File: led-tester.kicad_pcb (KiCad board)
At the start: 2 copper layers, 79.7 x 19.1 mm, 19 parts, among them M1 Arduino_Mini, U1 PCF8591

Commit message: Added a current sense resistor, a decoupling cap, and rewired the PCF8591 analog inputs.
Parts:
- added C2: 100n, Capacitor_SMD:C_0805_2012Metric_Pad1.18x1.45mm_HandSolder, F.Cu at (162.1, 88.8)
- added R7: 4R7, Resistor_SMD:R_0805_2012Metric_Pad1.20x1.40mm_HandSolder, F.Cu at (162.1, 83.9)
- D4: footprint aalib:LED_D5.0mm -> Connector_PinHeader_2.54mm:PinHeader_1x02_P2.54mm_Vertical
- D5: footprint Connector_PinHeader_2.54mm:PinHeader_1x02_P2.54mm_Vertical -> aalib:LED_D5.0mm
- JP2, JP3: moved to B.Cu
- moved R1 9.90 mm to (153.6, 83.9), turned to 0 degrees
- moved R3 5.35 mm to (157.8, 83.9)
- moved D4 5.10 mm to (169.9, 90.1), turned to -90 degrees
- moved D5 5.05 mm to (169.8, 85.0), turned to 180 degrees
- moved JP2 3.70 mm to (155.4, 83.9), turned to 180 degrees
- moved JP3 3.70 mm to (152.1, 83.9)
- moved D6 2.70 mm to (162.1, 86.3)
- moved R2 1.10 mm to (162.1, 93.5)
- moved R4 1.10 mm to (162.1, 91.2)
- moved D3 0.14 mm to (168.6, 93.2)
- moved D2 0.09 mm to (168.6, 95.7)
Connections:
- C1 pad 1: /A0 -> /A2
- D1 pad 2: /VLED -> /A0
- D2 pad 2: /VLED -> /A0
- D3 pad 2: /VLED -> /A0
- D4 pad 2: /VLED -> /A0
- D5 pad 2: /VLED -> /A0
- JP1 pad 2: /VLED -> /A0
- JP2 pad 1: /A1 -> Net-(JP2-A)
- JP2 pad 2: /VLED -> /A1
- JP3 pad 2: /VLED -> /A1
- R1 pad 2: /A0 -> /A2
- R2 pad 2: /A0 -> /A2
- R3 pad 1: /A1 -> Net-(JP2-A)
- R3 pad 2: /A0 -> /A2
- U1 pad 2: /A0 -> /A1
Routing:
- net /A2: track 0.00 -> 73.6 mm
- net /VLED: track 42.0 -> 0.00 mm, vias 1 -> 0
- net /A0: track 110.7 -> 90.8 mm
- net /*D3: track 40.4 -> 24.1 mm
- net GND: track 81.9 -> 90.2 mm
- net Net-(D6-A): track 3.20 -> 8.02 mm
- net /A1: track 55.5 -> 59.9 mm, vias 1 -> 3
- net Net-(JP2-A): track 0.00 -> 2.09 mm, vias 0 -> 1
- net Net-(JP3-A): track 4.96 -> 6.85 mm, vias 0 -> 1
- net +5V: track 39.8 -> 41.4 mm
- net /A5/SCL: track 36.2 -> 36.8 mm
- net /D13/SCK: track 60.2 -> 59.7 mm
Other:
- board text added: "2-May-23"
- board text added: "mjd v1.0d"
- board text added: "nano"
- board text removed: "24-Feb-23"
- board text removed: "mjd v1.0c"

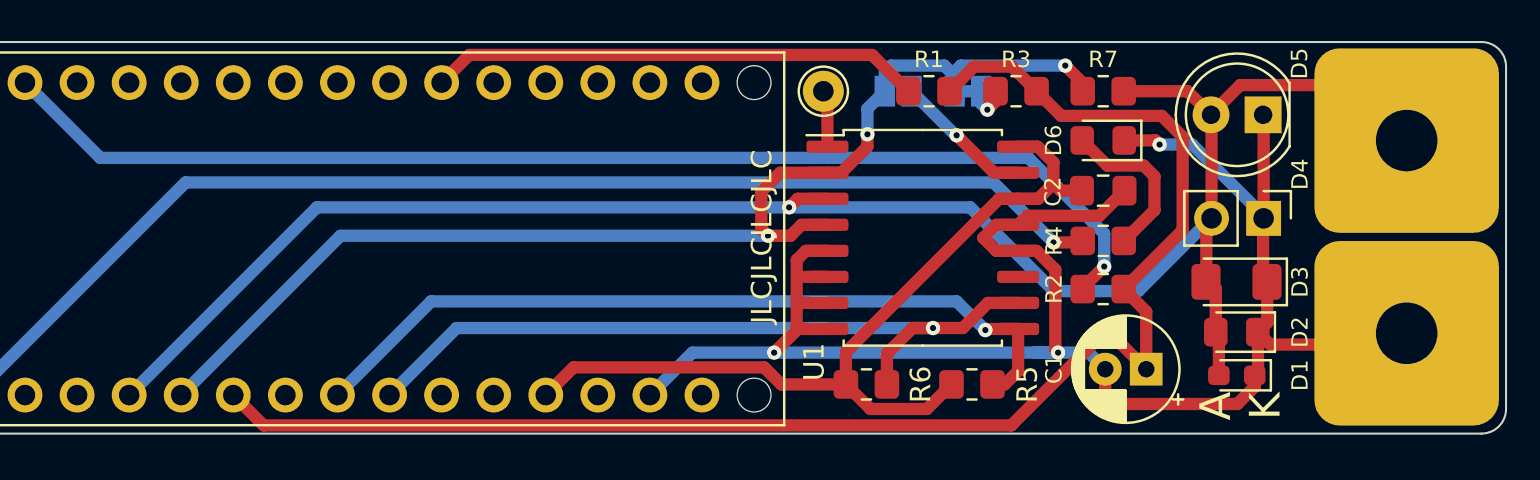
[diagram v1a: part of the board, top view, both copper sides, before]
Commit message: Added a sense resistor between the LED under test, and GND.
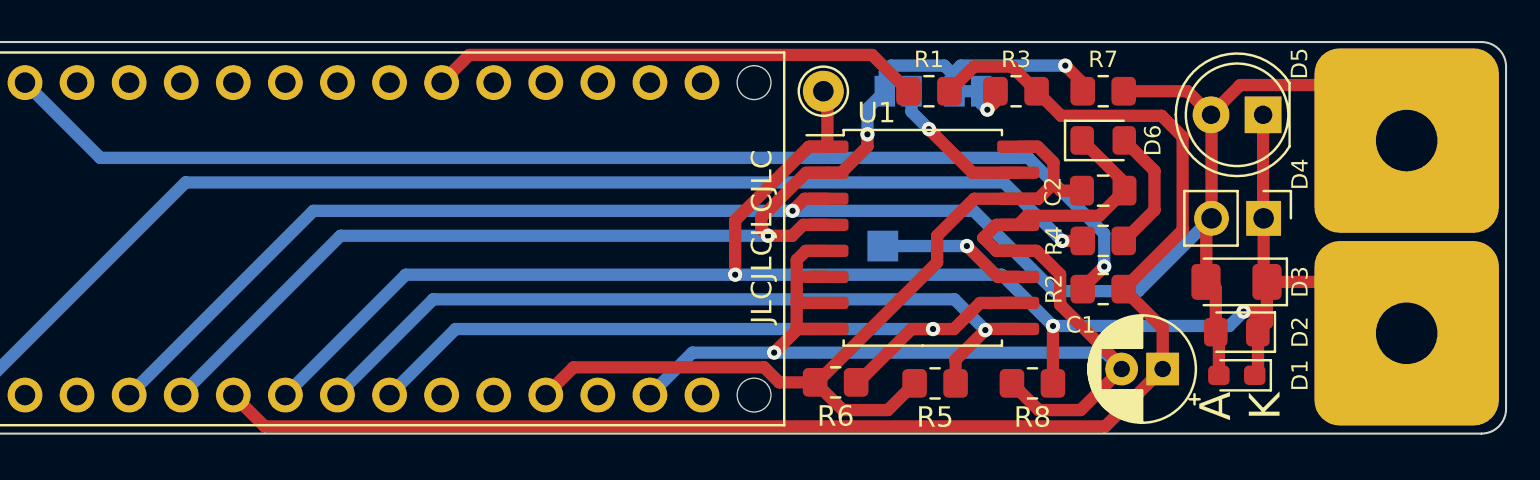
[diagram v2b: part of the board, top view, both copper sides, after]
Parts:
- added R8: 4R7, Resistor_SMD:R_0805_2012Metric_Pad1.20x1.40mm_HandSolder, F.Cu at (158.6, 98.2)
- added TP2: TestPoint, TestPoint:TestPoint_Pad_1.5x1.5mm, B.Cu at (151.3, 91.5)
- moved R5 1.80 mm to (153.8, 98.2)
- moved R6 1.50 mm to (149.0, 98.1)
- moved C1 0.80 mm to (164.9, 97.5)
- turned D6 to 0 degrees
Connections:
- D1 pad 1: GND -> /A3
- D2 pad 1: GND -> /A3
- D3 pad 1: GND -> /A3
- D4 pad 1: GND -> /A3
- D5 pad 1: GND -> /A3
- JP1 pad 1: GND -> /A3
- TP1 pad 1: Net-(U1-AIN0) -> /A3
- U1 pad 1: Net-(U1-AIN0) -> /A3
- U1 pad 11: unconnected-(U1-OSC-Pad11) -> Net-(U1-OSC)
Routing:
- net /A3: track 0.00 -> 86.8 mm, vias 0 -> 3
- net GND: track 90.2 -> 63.2 mm, vias 3 -> 1
- net Net-(U1-OSC): track 0.00 -> 7.22 mm, vias 0 -> 1
- net Net-(U1-AIN0): track 2.79 -> 0.00 mm
- net Net-(D6-A): track 8.02 -> 6.13 mm
- net /A1: track 59.9 -> 59.2 mm
- net Net-(JP3-A): track 6.85 -> 7.43 mm
- net /A5/SCL: track 36.8 -> 37.3 mm
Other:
- board text added: "4-May-23"
- board text added: "mjd v1.0e"
- board text removed: "2-May-23"
- board text removed: "mjd v1.0d"

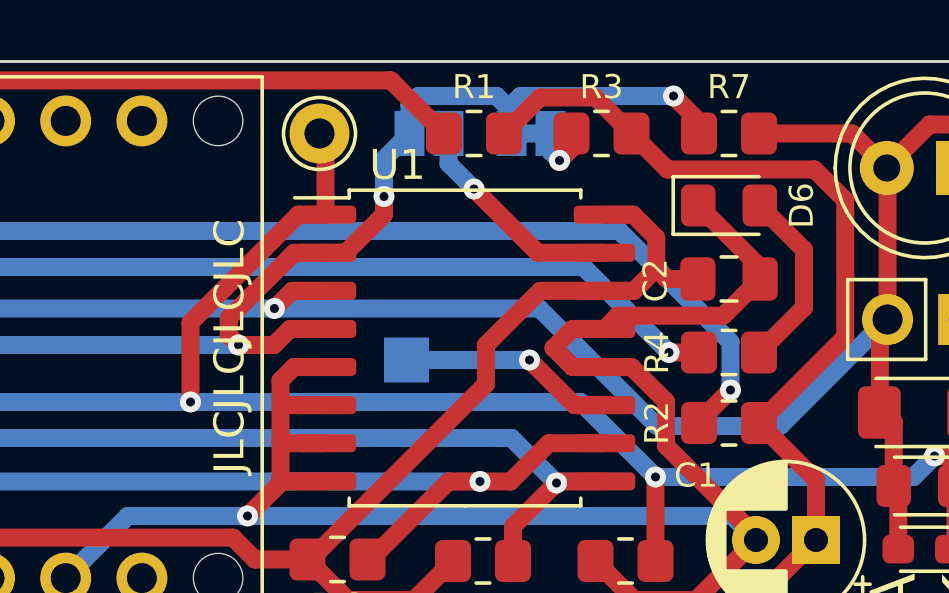
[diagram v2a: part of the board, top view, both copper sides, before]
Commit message: Added .gitignore, changed output directory.
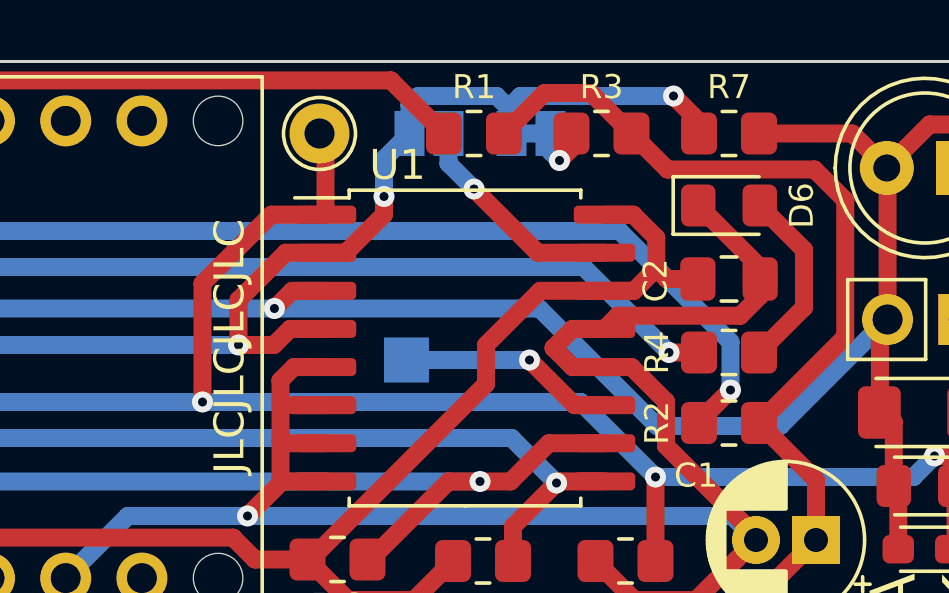
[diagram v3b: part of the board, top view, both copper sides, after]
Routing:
- net /A3: track 86.8 -> 87.6 mm
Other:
- board text added: "11-May-23"
- board text added: "mjd v1.0f"
- board text removed: "4-May-23"
- board text removed: "mjd v1.0e"
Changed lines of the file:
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@@
       (drillshape 0)
       (scaleselection 1)
-      (outputdirectory "outputs/")
+      (outputdirectory "output/")
     )
   )
@@
   (gr_arc (start 181.7 99.4) (mid 181.348528 100.248528) (end 180.5 100.6)
     (stroke (width 0.1) (type solid)) (layer "Edge.Cuts"))
-  (gr_text "mjd v1.0e" (at 169.050002 95.956482 90) (layer "B.SilkS")
+  (gr_text "mjd v1.0f" (at 169.050002 95.956482 90) (layer "B.SilkS")
     (effects (font (size 1 1) (thickness 0.15)) (justify mirror))
   )
-  (gr_text "4-May-23" (at 170.750002 95.956482 90) (layer "B.SilkS")
+  (gr_text "11-May-23" (at 170.750002 95.956482 90) (layer "B.SilkS")
     (effects (font (size 1 1) (thickness 0.15)) (justify mirror))
   )
@@
   (segment (start 148.6 95.495) (end 147.195 95.495) (width 0.6) (layer "F.Cu") (net 1))
   (segment (start 157.6 98.15) (end 158.9 99.45) (width 0.6) (layer "F.Cu") (net 1))
-  (segment (start 161.8625 89.975) (end 163.0875 88.75) (width 0.6) (layer "F.Cu") (net 1))
+  (segment (start 162.425 89.975) (end 163.0875 89.3125) (width 0.6) (layer "F.Cu") (net 1))
   (segment (start 157.9 91.685) (end 158.8 91.685) (width 0.6) (layer "F.Cu") (net 1))
   (segment (start 148.6 91.685) (end 147.545666 91.685) (width 0.6) (layer "F.Cu") (net 1))
@@
   (segment (start 148.6 92.955) (end 147.505 92.955) (width 0.6) (layer "F.Cu") (net 1))
   (segment (start 148.6 94.225) (end 147.175 94.225) (width 0.6) (layer "F.Cu") (net 1))
+  (segment (start 163.0875 89.3125) (end 163.0875 88.75) (width 0.6) (layer "F.Cu") (net 1))
   (segment (start 147.1 92.130666) (end 147.1 94.15) (width 0.6) (layer "F.Cu") (net 1))
   (segment (start 156.2 91.05) (end 156.835 90.415) (width 0.6) (layer "F.Cu") (net 1))
+  (segment (start 158.34 89.975) (end 162.425 89.975) (width 0.6) (layer "F.Cu") (net 1))
   (segment (start 159.95 92.835) (end 159.95 94.31066) (width 0.6) (layer "F.Cu") (net 1))
   (segment (start 147.175 94.225) (end 147.1 94.15) (width 0.6) (layer "F.Cu") (net 1))
   (segment (start 158.8 91.685) (end 159.95 92.835) (width 0.6) (layer "F.Cu") (net 1))
+  (segment (start 157.9 90.415) (end 158.34 89.975) (width 0.6) (layer "F.Cu") (net 1))
   (segment (start 160.95 99.45) (end 162.95 97.45) (width 0.6) (layer "F.Cu") (net 1))
   (segment (start 147.1 94.15) (end 147.1 95.4) (width 0.6) (layer "F.Cu") (net 1))
@@
   (segment (start 158.9 99.45) (end 160.95 99.45) (width 0.6) (layer "F.Cu") (net 1))
   (segment (start 157.9 91.685) (end 156.835 91.685) (width 0.6) (layer "F.Cu") (net 1))
-  (segment (start 158.34 89.975) (end 161.8625 89.975) (width 0.6) (layer "F.Cu") (net 1))
   (segment (start 159.95 94.31066) (end 162.95 97.31066) (width 0.6) (layer "F.Cu") (net 1))
-  (segment (start 157.9 90.415) (end 158.34 89.975) (width 0.6) (layer "F.Cu") (net 1))
   (segment (start 163.0875 88.75) (end 163.0875 88.3625) (width 0.6) (layer "F.Cu") (net 1))
   (via (at 146 96.650001) (size 0.7) (drill 0.3) (layers "F.Cu" "B.Cu") (net 1))
@@
   (segment (start 170.0375 95.205002) (end 169.592502 95.65) (width 0.6) (layer "F.Cu") (net 11))
   (segment (start 148.6 84.1) (end 148.4 83.9) (width 0.6) (layer "F.Cu") (net 11))
-  (segment (start 148.6 86.605) (end 147.694296 86.605) (width 0.6) (layer "F.Cu") (net 11))
-  (segment (start 144.1 90.199296) (end 144.1 92.850002) (width 0.6) (layer "F.Cu") (net 11))
   (segment (start 174.344992 93.2) (end 176.851474 95.706482) (width 0.6) (layer "F.Cu") (net 11))
   (segment (start 148.6 86.605) (end 148.6 84.1) (width 0.6) (layer "F.Cu") (net 11))
@@
   (segment (start 168.9 94.65) (end 169.9375 94.65) (width 0.6) (layer "F.Cu") (net 11))
   (segment (start 169.442502 97.756482) (end 169.6 97.598984) (width 0.6) (layer "F.Cu") (net 11))
-  (segment (start 147.694296 86.605) (end 144.1 90.199296) (width 0.6) (layer "F.Cu") (net 11))
   (segment (start 169.6 97.598984) (end 169.6 95.657498) (width 0.6) (layer "F.Cu") (net 11))
+  (segment (start 148.6 86.605) (end 146.795 86.605) (width 0.6) (layer "F.Cu") (net 11))
   (segment (start 159.6 98.15) (end 159.6 95.35) (width 0.6) (layer "F.Cu") (net 11))
+  (segment (start 146.795 86.605) (end 144.5 88.9) (width 0.6) (layer "F.Cu") (net 11))
+  (segment (start 144.5 88.9) (end 144.5 92.85) (width 0.6) (layer "F.Cu") (net 11))
   (segment (start 170.0375 93.2) (end 174.344992 93.2) (width 0.6) (layer "F.Cu") (net 11))
   (segment (start 169.6 95.657498) (end 169.592502 95.65) (width 0.6) (layer "F.Cu") (net 11))
   (via (at 168.9 94.65) (size 0.7) (drill 0.3) (layers "F.Cu" "B.Cu") (net 11))
-  (via (at 144.1 92.850002) (size 0.7) (drill 0.3) (layers "F.Cu" "B.Cu") (net 11))
+  (via (at 144.5 92.85) (size 0.7) (drill 0.3) (layers "F.Cu" "B.Cu") (net 11))
   (via (at 159.6 95.35) (size 0.7) (drill 0.3) (layers "F.Cu" "B.Cu") (net 11))
   (segment (start 157.1 92.85) (end 159.6 95.35) (width 0.6) (layer "B.Cu") (net 11))
-  (segment (start 144.1 92.85) (end 144.1 92.850002) (width 0.6) (layer "B.Cu") (net 11))
+  (segment (start 144.1 92.85) (end 144.5 92.85) (width 0.6) (layer "B.Cu") (net 11))
   (segment (start 128.03 92.85) (end 144.1 92.85) (width 0.6) (layer "B.Cu") (net 11))
   (segment (start 168.2 95.35) (end 168.9 94.65) (width 0.6) (layer "B.Cu") (net 11))
@@
   (segment (start 159.6 95.35) (end 168.2 95.35) (width 0.6) (layer "B.Cu") (net 11))
   (segment (start 164.95 95.45) (end 163.05 93.55) (width 0.6) (layer "F.Cu") (net 12))
-  (segment (start 154.55 83.9) (end 155.75 82.7) (width 0.6) (layer "F.Cu") (net 12))
-  (segment (start 155.75 82.7) (end 157.6 82.7) (width 0.6) (layer "F.Cu") (net 12))
   (segment (start 164.9 85.1) (end 160 85.1) (width 0.6) (layer "F.Cu") (net 12))
   (segment (start 121.149501 100.249501) (end 162.150499 100.249501) (width 0.6) (layer "F.Cu") (net 12))
@@
   (segment (start 163.05 93.55) (end 165.925 90.675) (width 0.6) (layer "F.Cu") (net 12))
   (segment (start 119.62 98.72) (end 121.149501 100.249501) (width 0.6) (layer "F.Cu") (net 12))
-  (segment (start 157.6 82.7) (end 158.8 83.9) (width 0.6) (layer "F.Cu") (net 12))
+  (segment (start 154.55 83.9) (end 155.9 82.55) (width 0.6) (layer "F.Cu") (net 12))
   (segment (start 160 85.1) (end 158.8 83.9) (width 0.6) (layer "F.Cu") (net 12))
+  (segment (start 157.45 82.55) (end 158.8 83.9) (width 0.6) (layer "F.Cu") (net 12))
   (segment (start 165.925 90.675) (end 165.925 86.125) (width 0.6) (layer "F.Cu") (net 12))
   (segment (start 164.95 97.45) (end 164.95 95.45) (width 0.6) (layer "F.Cu") (net 12))
   (segment (start 162.150499 100.249501) (end 164.95 97.45) (width 0.6) (layer "F.Cu") (net 12))
+  (segment (start 155.9 82.55) (end 157.45 82.55) (width 0.6) (layer "F.Cu") (net 12))
   (segment (start 147.417713 90.415) (end 146.882713 90.95) (width 0.6) (layer "F.Cu") (net 13))
   (segment (start 161.05 83.9) (end 161.05 83.5) (width 0.6) (layer "F.Cu") (net 13))
-  (segment (start 147.554962 87.875) (end 148.6 87.875) (width 0.6) (layer "F.Cu") (net 13))
   (segment (start 161.05 83.5) (end 160.2 82.65) (width 0.6) (layer "F.Cu") (net 13))
   (segment (start 149.274239 87.875) (end 150.55 86.599239) (width 0.6) (layer "F.Cu") (net 13))
-  (segment (start 145.7 90.95) (end 145.3755 90.6255) (width 0.6) (layer "F.Cu") (net 13))
+  (segment (start 145.7 89.45) (end 147.275 87.875) (width 0.6) (layer "F.Cu") (net 13))
+  (segment (start 147.275 87.875) (end 148.6 87.875) (width 0.6) (layer "F.Cu") (net 13))
   (segment (start 148.6 87.875) (end 149.274239 87.875) (width 0.6) (layer "F.Cu") (net 13))
   (segment (start 148.6 90.415) (end 147.417713 90.415) (width 0.6) (layer "F.Cu") (net 13))
+  (segment (start 145.7 90.95) (end 145.7 89.45) (width 0.6) (layer "F.Cu") (net 13))
   (segment (start 150.55 86.599239) (end 150.55 86) (width 0.6) (layer "F.Cu") (net 13))
-  (segment (start 145.3755 90.6255) (end 145.3755 90.054462) (width 0.6) (layer "F.Cu") (net 13))
   (segment (start 146.882713 90.95) (end 145.7 90.95) (width 0.6) (layer "F.Cu") (net 13))
-  (segment (start 145.3755 90.054462) (end 147.554962 87.875) (width 0.6) (layer "F.Cu") (net 13))
   (via (at 145.7 90.95) (size 0.7) (drill 0.3) (layers "F.Cu" "B.Cu") (net 13))
   (via (at 150.55 86) (size 0.7) (drill 0.3) (layers "F.Cu" "B.Cu") (net 13))
